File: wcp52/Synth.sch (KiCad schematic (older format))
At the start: 52 parts, among them U2 LMH6714MF, U3 AD9958BCPZ, U4 LMH6714MF, X1 25 MHz

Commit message: Prepare to fab
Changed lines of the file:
@@
 $EndComp
 Wire Wire Line
-	3350 1950 3350 2000
-Wire Wire Line
-	3350 2000 3350 2100
-Wire Wire Line
-	3350 2000 3450 2000
-Wire Wire Line
-	3450 2000 3550 2000
-Wire Wire Line
-	3550 2000 3650 2000
-Wire Wire Line
-	3650 2000 3750 2000
-Wire Wire Line
-	3750 2000 3850 2000
-Wire Wire Line
-	3850 2000 3950 2000
-Wire Wire Line
-	3950 2000 4050 2000
-Wire Wire Line
-	4050 2000 4150 2000
-Wire Wire Line
-	4150 2000 4250 2000
-Wire Wire Line
-	4250 2000 4350 2000
-Wire Wire Line
-	4350 2000 4450 2000
-Wire Wire Line
-	4450 2000 4550 2000
-Wire Wire Line
-	4550 2000 4650 2000
-Wire Wire Line
-	4650 2000 4750 2000
+	3350 1950 3350 2100
+Wire Wire Line
+	3350 2000 4750 2000
 Wire Wire Line
 	4750 2000 4750 2100
@@
 Connection ~ 3450 2000
 Wire Wire Line
-	4950 1950 4950 2000
-Wire Wire Line
-	4950 2000 4950 2100
+	4950 1950 4950 2100
 Wire Wire Line
 	4950 2000 5050 2000
@@
 	3050 2800 1600 2800
 Wire Wire Line
-	1950 3000 2300 3000
-Wire Wire Line
-	2300 3000 3050 3000
-Wire Wire Line
-	1950 3300 2300 3300
-Wire Wire Line
-	2300 3300 2550 3300
+	1950 3000 3050 3000
+Wire Wire Line
+	1950 3300 2550 3300
 Wire Wire Line
 	2550 3300 2550 3100
@@
 	1750 3000 1650 3000
 Wire Wire Line
-	1650 3000 1650 3150
-Wire Wire Line
-	1650 3150 1650 3300
+	1650 3000 1650 3300
 Wire Wire Line
 	1650 3300 1750 3300
@@
 	3050 3800 2950 3800
 Wire Wire Line
-	2950 3800 2950 3900
-Wire Wire Line
-	2950 3900 2950 4000
-Wire Wire Line
-	2950 4000 2950 4100
-Wire Wire Line
-	2950 4100 2950 4150
+	2950 3800 2950 4150
 Wire Wire Line
 	2950 4100 3050 4100
@@
 	5550 2550 5550 2700
 Wire Wire Line
-	7250 2700 5550 2700
-Wire Wire Line
-	5550 2700 5450 2700
+	7250 2700 5450 2700
 Wire Wire Line
 	5750 2550 5750 2800
 Wire Wire Line
-	7350 2800 5750 2800
-Wire Wire Line
-	5750 2800 5450 2800
+	7350 2800 5450 2800
 Wire Wire Line
 	6050 2550 6050 3000
 Wire Wire Line
-	5450 3000 6050 3000
-Wire Wire Line
-	6050 3000 6450 3000
+	5450 3000 6450 3000
 Wire Wire Line
 	6250 2550 6250 3100
 Wire Wire Line
-	5450 3100 6250 3100
-Wire Wire Line
-	6250 3100 6350 3100
+	5450 3100 6350 3100
 Wire Wire Line
 	5550 2350 5550 2250
 Wire Wire Line
-	5550 2250 5650 2250
-Wire Wire Line
-	5650 2250 5750 2250
+	5550 2250 5750 2250
 Wire Wire Line
 	5750 2250 5750 2350
@@
 	6050 2350 6050 2250
 Wire Wire Line
-	6050 2250 6150 2250
-Wire Wire Line
-	6150 2250 6250 2250
+	6050 2250 6250 2250
 Wire Wire Line
 	6250 2250 6250 2350
@@
 	7250 1200 7250 1100
 Wire Wire Line
-	7250 1100 7300 1100
-Wire Wire Line
-	7300 1100 7350 1100
+	7250 1100 7350 1100
 Wire Wire Line
 	7350 1100 7350 1200
@@
 Connection ~ 7300 1100
 Wire Wire Line
-	7250 1400 7250 1500
-Wire Wire Line
-	7250 1500 7250 2700
-Wire Wire Line
-	7350 1400 7350 2200
-Wire Wire Line
-	7350 2200 7350 2800
+	7250 1400 7250 2700
+Wire Wire Line
+	7350 1400 7350 2800
 Connection ~ 5750 2800
 Wire Wire Line
@@
 Connection ~ 7250 1500
 Wire Wire Line
-	7850 1500 8050 1500
-Wire Wire Line
-	8050 1500 8550 1500
+	7850 1500 8550 1500
 Wire Wire Line
 	7650 2200 7350 2200
 Connection ~ 7350 2200
 Wire Wire Line
-	7850 2200 8050 2200
-Wire Wire Line
-	8050 2200 8550 2200
+	7850 2200 8550 2200
 Wire Wire Line
 	8250 1750 8050 1750
@@
 Connection ~ 8050 2200
 Wire Wire Line
-	8750 1500 8850 1500
-Wire Wire Line
-	8850 1500 9050 1500
-Wire Wire Line
-	8850 1500 8850 1850
-Wire Wire Line
-	8850 1850 8850 2250
+	8750 1500 9050 1500
+Wire Wire Line
+	8850 1500 8850 2250
 Wire Wire Line
 	8850 1850 8750 1850
@@
 	9800 1500 9250 1500
 Wire Wire Line
-	9700 1550 9700 2200
-Wire Wire Line
-	9700 2200 9700 2250
+	9700 1550 9700 2250
 Wire Wire Line
 	9700 2200 8750 2200
@@
 	7250 3200 7250 3100
 Wire Wire Line
-	7250 3100 7300 3100
-Wire Wire Line
-	7300 3100 7350 3100
+	7250 3100 7350 3100
 Wire Wire Line
 	7350 3100 7350 3200
@@
 	7650 3500 7250 3500
 Wire Wire Line
-	7850 3500 8050 3500
-Wire Wire Line
-	8050 3500 8550 3500
+	7850 3500 8550 3500
 Wire Wire Line
 	7650 4200 7350 4200
 Wire Wire Line
-	7850 4200 8050 4200
-Wire Wire Line
-	8050 4200 8550 4200
+	7850 4200 8550 4200
 Wire Wire Line
 	8250 3750 8050 3750
@@
 Connection ~ 8050 4200
 Wire Wire Line
-	8750 3500 8850 3500
-Wire Wire Line
-	8850 3500 9050 3500
-Wire Wire Line
-	8850 3500 8850 3850
-Wire Wire Line
-	8850 3850 8850 4250
+	8750 3500 9050 3500
+Wire Wire Line
+	8850 3500 8850 4250
 Wire Wire Line
 	8850 3850 8750 3850
@@
 	9800 3500 9250 3500
 Wire Wire Line
-	9700 3550 9700 4200
-Wire Wire Line
-	9700 4200 9700 4250
+	9700 3550 9700 4250
 Wire Wire Line
 	9700 4200 8750 4200
 Connection ~ 9700 4200
 Wire Wire Line
-	7250 3400 7250 3500
-Wire Wire Line
-	7250 3500 7250 4400
+	7250 3400 7250 4400
 Wire Wire Line
 	7250 4400 6450 4400
@@
 	6350 3100 6350 4500
 Wire Wire Line
-	6350 4500 7350 4500
-Wire Wire Line
-	7350 4500 7350 4200
-Wire Wire Line
-	7350 4200 7350 3400
+	7350 4500 6350 4500
+Wire Wire Line
+	7350 3400 7350 4500
 Connection ~ 6250 3100
 Connection ~ 7250 3500
@@
 	7900 6300 7900 6250
 Wire Wire Line
-	8300 6050 8300 6150
-Wire Wire Line
-	8300 6150 8300 6250
+	8300 6050 8300 6250
 $Comp
 L GND #PWR097
@@
 	9100 6300 9100 6250
 Wire Wire Line
-	9500 6050 9500 6150
-Wire Wire Line
-	9500 6150 9500 6250
+	9500 6050 9500 6250
 $Comp
 L GND #PWR0104
@@
 $EndComp
 Wire Wire Line
-	10000 6050 10000 6150
-Wire Wire Line
-	10000 6150 10000 6250
+	10000 6050 10000 6250
 $Comp
 L GND #PWR0107

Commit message: BOM line fixes
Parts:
- C10, C11, C12, C13, C14, C15, C16, C17, C18, C19, C20, C21, C22, C23, C24, C25, C26, C27, C28, C29, C30, C31, C8, C9, R18, R19, R20, R21, R22, R23, R24, R25, R26, R27, R28, R29, R30, R31, R32, R33, R34, R35, R36, R37, R38, R39, U2, U3, U4: Manuf Value -> (none)
- E2: Description (none) -> FERRITE CHIP 2.2k @ 100MHz [0805]
- X1: Description (none) -> CRYSTAL 25MHz 18pF 10PPM; Manuf Value -> TXC; PN (none) -> 9C-25.000MEEJ-T

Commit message: BOM corrections/combinations, etc
Add configuration for bomtool
Remove old schematic file no longer used
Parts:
- U2, U4: BOM DIST DIGIKEY LMH6714MF/NOPBCT-ND -> (none)
- U3: BOM #DIST DIGIKEY AD9958BCPZ-ND -> IC ADI AD9958BCPZ
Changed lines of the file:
@@
 F 2 "manuf:ANALOG-LFCSP-VQ-56" H 4250 3650 50  0001 C CNN
 F 3 "" H 2200 3350 60  0000 C CNN
-F 4 "" H 4250 3650 60  0001 C CNN "Manuf"
-F 5 "#DIST DIGIKEY AD9958BCPZ-ND" H 4700 4200 60  0001 C CNN "BOM"
-F 6 "U4" H 4250 3650 50  0001 C CNN "OldReference"
+F 4 "IC ADI AD9958BCPZ" H 4700 4200 60  0001 C CNN "BOM"
+F 5 "U4" H 4250 3650 50  0001 C CNN "OldReference"
 	1    4250 3650
 	1    0    0    -1
@@
 F 2 "smd-semi:SOT-23-5" H 7600 5850 50  0001 C CNN
 F 3 "" H 7400 5850 60  0000 C CNN
-F 4 "DIST DIGIKEY LMH6714MF/NOPBCT-ND" H 8100 6700 60  0001 C CNN "BOM"
-F 5 "" H 7600 5850 60  0001 C CNN "Manuf"
-F 6 "U3" H 7600 5850 50  0001 C CNN "OldReference"
+F 4 "U3" H 7600 5850 50  0001 C CNN "OldReference"
 	2    7600 5850
 	1    0    0    -1
@@
 F 2 "smd-semi:SOT-23-5" H 8800 5850 50  0001 C CNN
 F 3 "" H 8600 5850 60  0000 C CNN
-F 4 "DIST DIGIKEY LMH6714MF/NOPBCT-ND" H 9300 6700 60  0001 C CNN "BOM"
-F 5 "" H 8800 5850 60  0001 C CNN "Manuf"
-F 6 "U5" H 8800 5850 50  0001 C CNN "OldReference"
+F 4 "U5" H 8800 5850 50  0001 C CNN "OldReference"
 	2    8800 5850
 	1    0    0    -1

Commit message: Schematic/doc work
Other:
- note added: "@R20 is copper-bridged on the PCB; it is not\nnecessary to populate a jumper. If this part\nmust be changed after testing, cut the bridge."
- note added: "Power supply decoupling\nThese are distributed among @U3's power pins."
- note added: "These decouple the amplifier\nends of the differential T-lines"
- note removed: "@R20 is copper-bridged on the PCB, it is not necessary to populate a jumper.\nIf this part must be changed after testing, cut the bridge."
- note removed: "These decouple the amplifier ends\nof the differential T-lines"
- moved on the sheet: E2

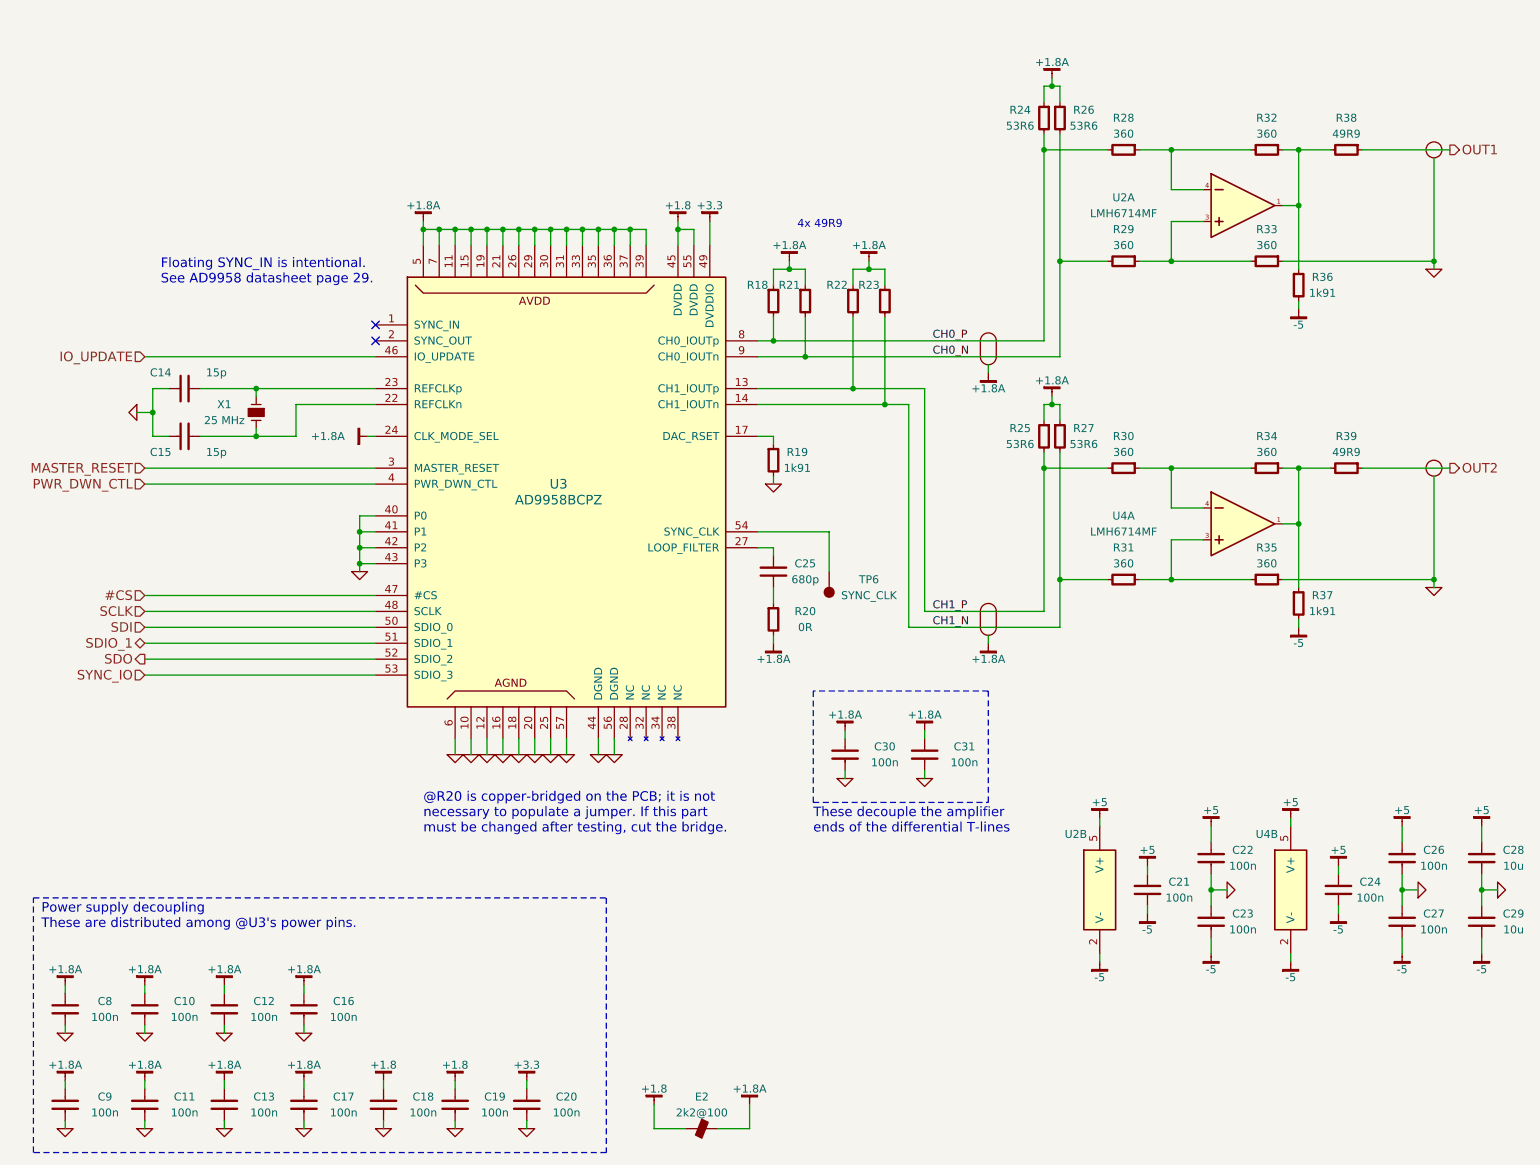
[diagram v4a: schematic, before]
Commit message: Schematic updates for documentation
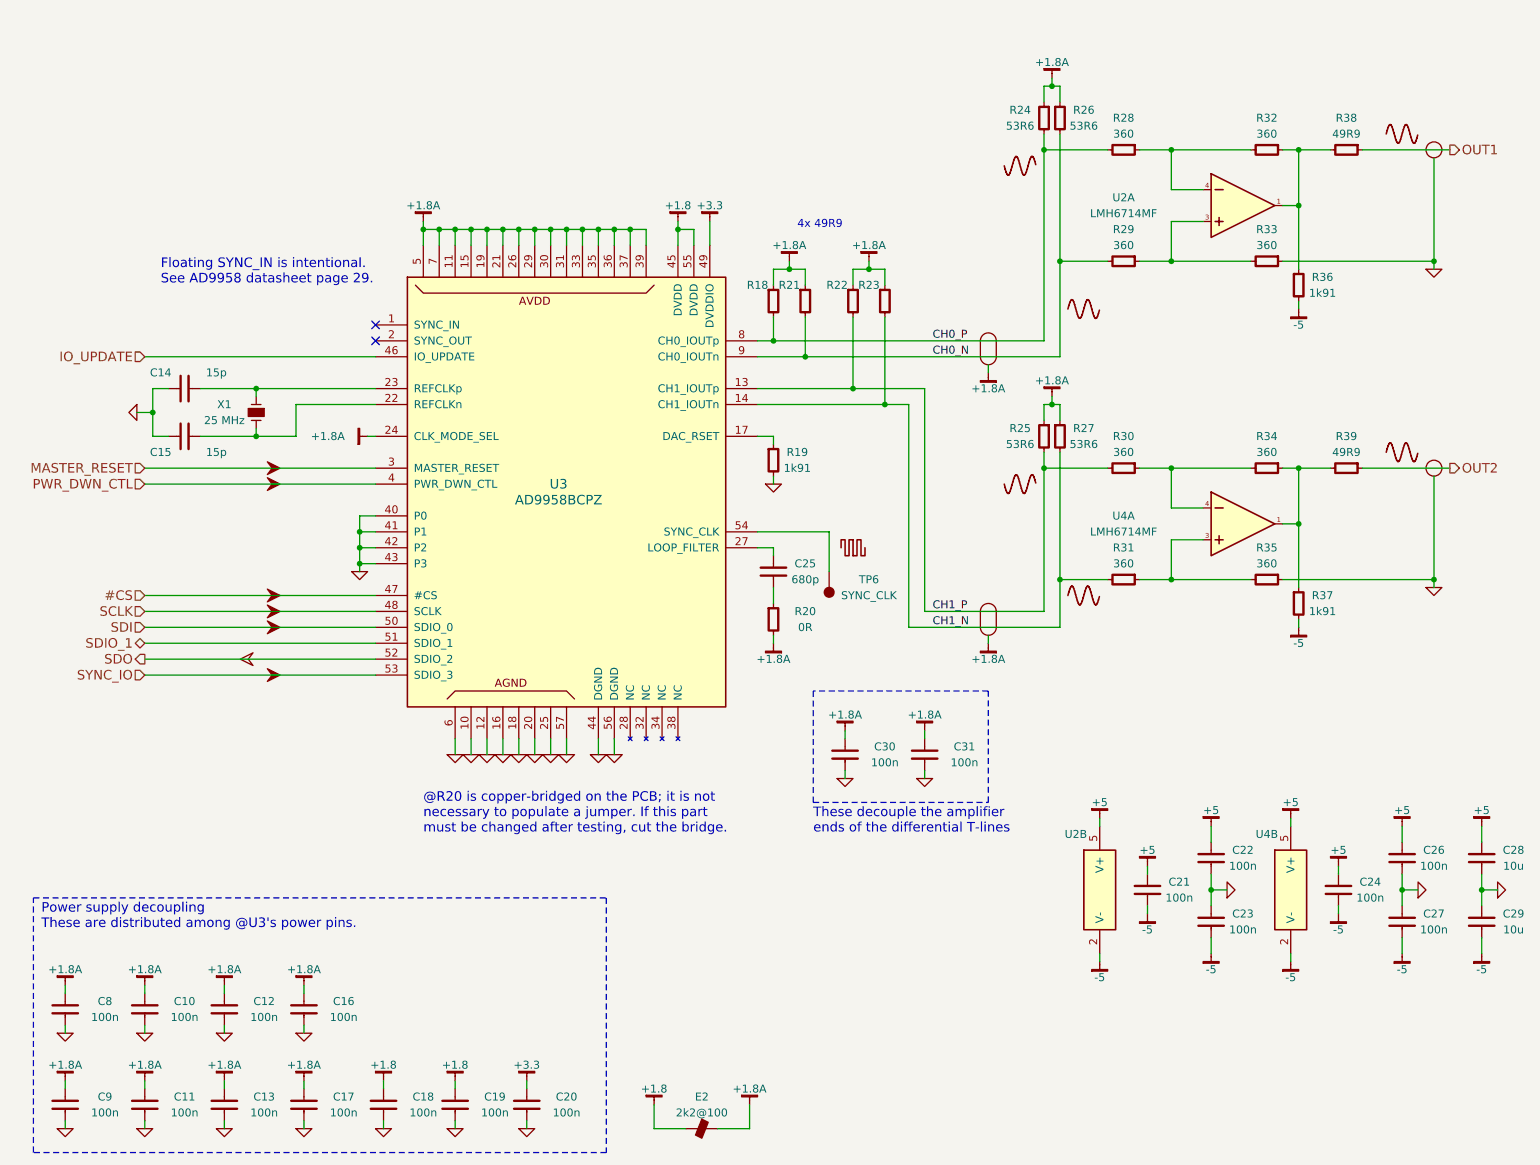
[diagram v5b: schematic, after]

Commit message: More doc fixes
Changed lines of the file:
@@
 	6400 3100 6400 4500
 Wire Wire Line
-	7350 4500 6400 4500
-Wire Wire Line
-	7350 3400 7350 4500
+	6400 4500 7350 4500
+Wire Wire Line
+	7350 4500 7350 3400
 Connection ~ 6250 3100
 Connection ~ 7250 3500
@@
 	1    0    0    -1
 $EndComp
+Wire Wire Line
+	9250 3500 9275 3525
+Wire Wire Line
+	9275 3525 9775 3525
+Wire Wire Line
+	9775 3525 9800 3500
+$Comp
+L SIGPATH_SM #SYM?
+U 1 1 5511C708
+P 2400 2800
+F 0 "#SYM?" H 2400 2800 60  0001 C CNN
+F 1 "SIGPATH_SM" H 2400 2800 60  0001 C CNN
+F 2 "" H 2400 2800 60  0000 C CNN
+F 3 "" H 2400 2800 60  0000 C CNN
+	1    2400 2800
+	1    0    0    -1
+$EndComp

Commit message: Nicer BOM lines
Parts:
- C10: OldReference C6 -> (none)
- C11: OldReference C14 -> (none)
- C12: OldReference C7 -> (none)
- C13: OldReference C15 -> (none)
- C14: OldReference C11 -> (none)
- C15: OldReference C12 -> (none)
- C16: OldReference C8 -> (none)
- C17: OldReference C16 -> (none)
- C18: OldReference C9 -> (none)
- C19: OldReference C17 -> (none)
- C20: OldReference C10 -> (none)
- C21: OldReference C19 -> (none)
- C22: OldReference C20 -> (none)
- C23: OldReference C21 -> (none)
- C24: OldReference C22 -> (none)
- C25: OldReference C23 -> (none)
- C26: OldReference C24 -> (none)
- C27: OldReference C25 -> (none)
- C28: OldReference C26 -> (none)
- C29: OldReference C27 -> (none)
- C30: OldReference C18 -> (none)
- C31: OldReference C55 -> (none)
- C8: OldReference C5 -> (none)
- C9: OldReference C13 -> (none)
- E2: OldReference E2 -> (none)
- R18: OldReference R13 -> (none)
- R19: OldReference R14 -> (none)
- R20: OldReference R12 -> (none)
- R21: OldReference R15 -> (none)
- R22: OldReference R17 -> (none)
- R23: OldReference R18 -> (none)
- R24: OldReference R19 -> (none)
- R25: OldReference R20 -> (none)
- R26: OldReference R21 -> (none)
- R27: OldReference R22 -> (none)
- R28: OldReference R23 -> (none)
- R29: OldReference R24 -> (none)
- R30: OldReference R25 -> (none)
- R31: OldReference R26 -> (none)
- R32: OldReference R27 -> (none)
- R33: OldReference R28 -> (none)
- R34: OldReference R29 -> (none)
- R35: OldReference R30 -> (none)
- R36: OldReference R31 -> (none)
- R37: OldReference R32 -> (none)
- R38: OldReference R33 -> (none)
- R39: OldReference R34 -> (none)
- TP6: OldReference TP2 -> (none)
- U2: OldReference U3 -> (none)
- U3: OldReference U4 -> (none)
- U4: OldReference U5 -> (none)
- X1: OldReference X1 -> (none)

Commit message: Add post-testing revision, todo notes
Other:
- note added: "TODO (REV 2):\nCorrection to U2/U4 differential amplifiers:\n- Input impedance is asymmetric so termination should also be.\n Change R24 and R25 to 57.6 ohms? Don't want to add a BOM item\n though, or make reactive loading asymmetric. Investigate..."
